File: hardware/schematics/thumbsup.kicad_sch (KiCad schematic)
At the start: 0 parts

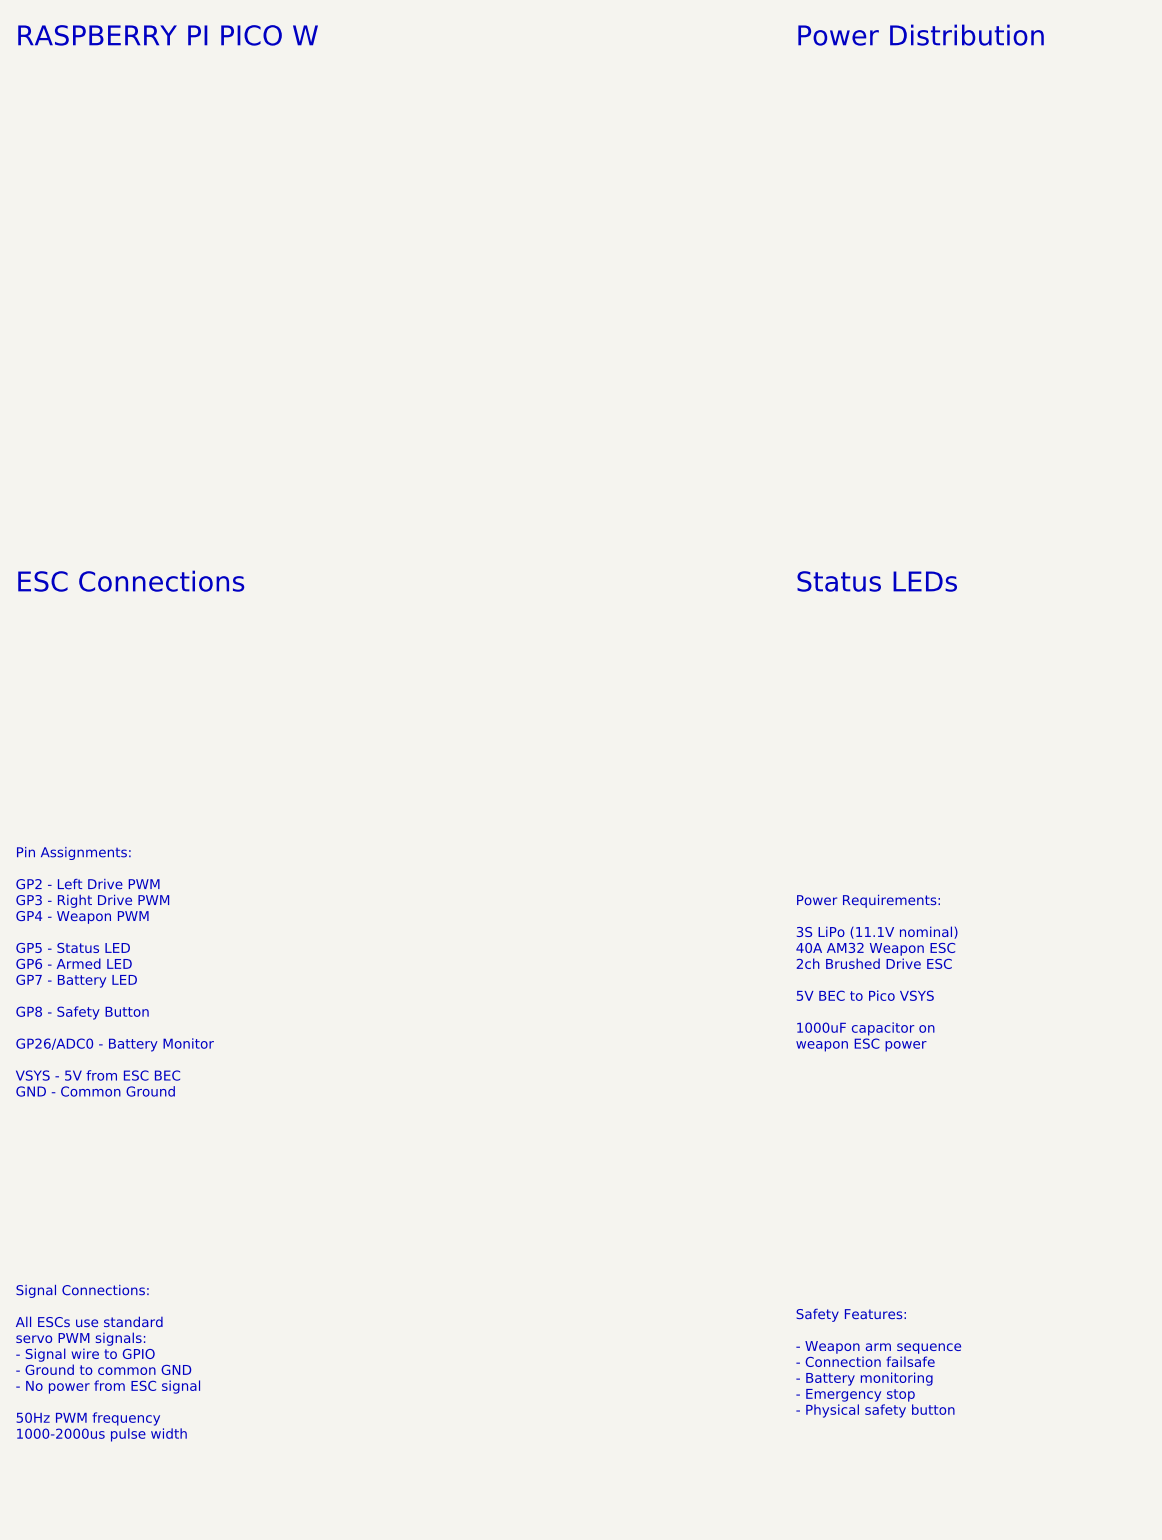
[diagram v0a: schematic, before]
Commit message: fix: Iteration 4 - Race conditions, buffer overflows, synchronization
This commit addresses all 4 CRITICAL and 7 MAJOR code quality issues
identified in the final pre-hardware testing review.

CRITICAL FIXES:

CRITICAL-1: Race condition in weapon_emergency_stop()
- Changed from mode-dependent stop to defense-in-depth approach
- Now executes ALL stop methods (PWM, DShot, GPIO) regardless of mode
- Prevents race where mode could change between read and execution
- Ensures motor stops even if one method fails

CRITICAL-2: Unprotected dshot_initialized flag access
- Made dshot_initialized volatile to prevent compiler reordering
- Flag already protected by mode_mutex in all modification paths
- Prevents use-after-free where weapon_update() could use freed DShot
  resources after mode switch calls dshot_deinit()

CRITICAL-3: Buffer overflow in am32_msp_receive()
- Added buffer_size parameter to function signature
- Validates payload_len from wire against caller's buffer size
- Prevents malicious ESC from overflowing buffer with large payload_len
- Added double-check bounds validation before each write

CRITICAL-4: Infinite loop in am32_passthrough_mode()
- Replaced blocking getchar() with getchar_timeout_us(1000)
- Prevents hang if interrupt consumes char between check and read
- Maintains passthrough functionality with non-blocking reads

MAJOR FIXES:

MAJOR-1: GPIO conflict window in mode switching
- Added comprehensive documentation of race window limitation
- Explained mitigation: single-threaded, mutex-protected, no ISR conflicts
- Added hardware testing requirements for validation

MAJOR-2: Missing NULL checks in dshot_send_throttle()
- Added NULL pointer check for state->pio before dereferencing
- Added validation that state->dma_chan >= 0 before use
- Prevents crashes if state is partially initialized

MAJOR-3: Integer overflow in dshot_throttle_from_percent()
- Rewrote formula to avoid negative intermediates
- Changed from: (percent * range)/100 + offset
- Change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
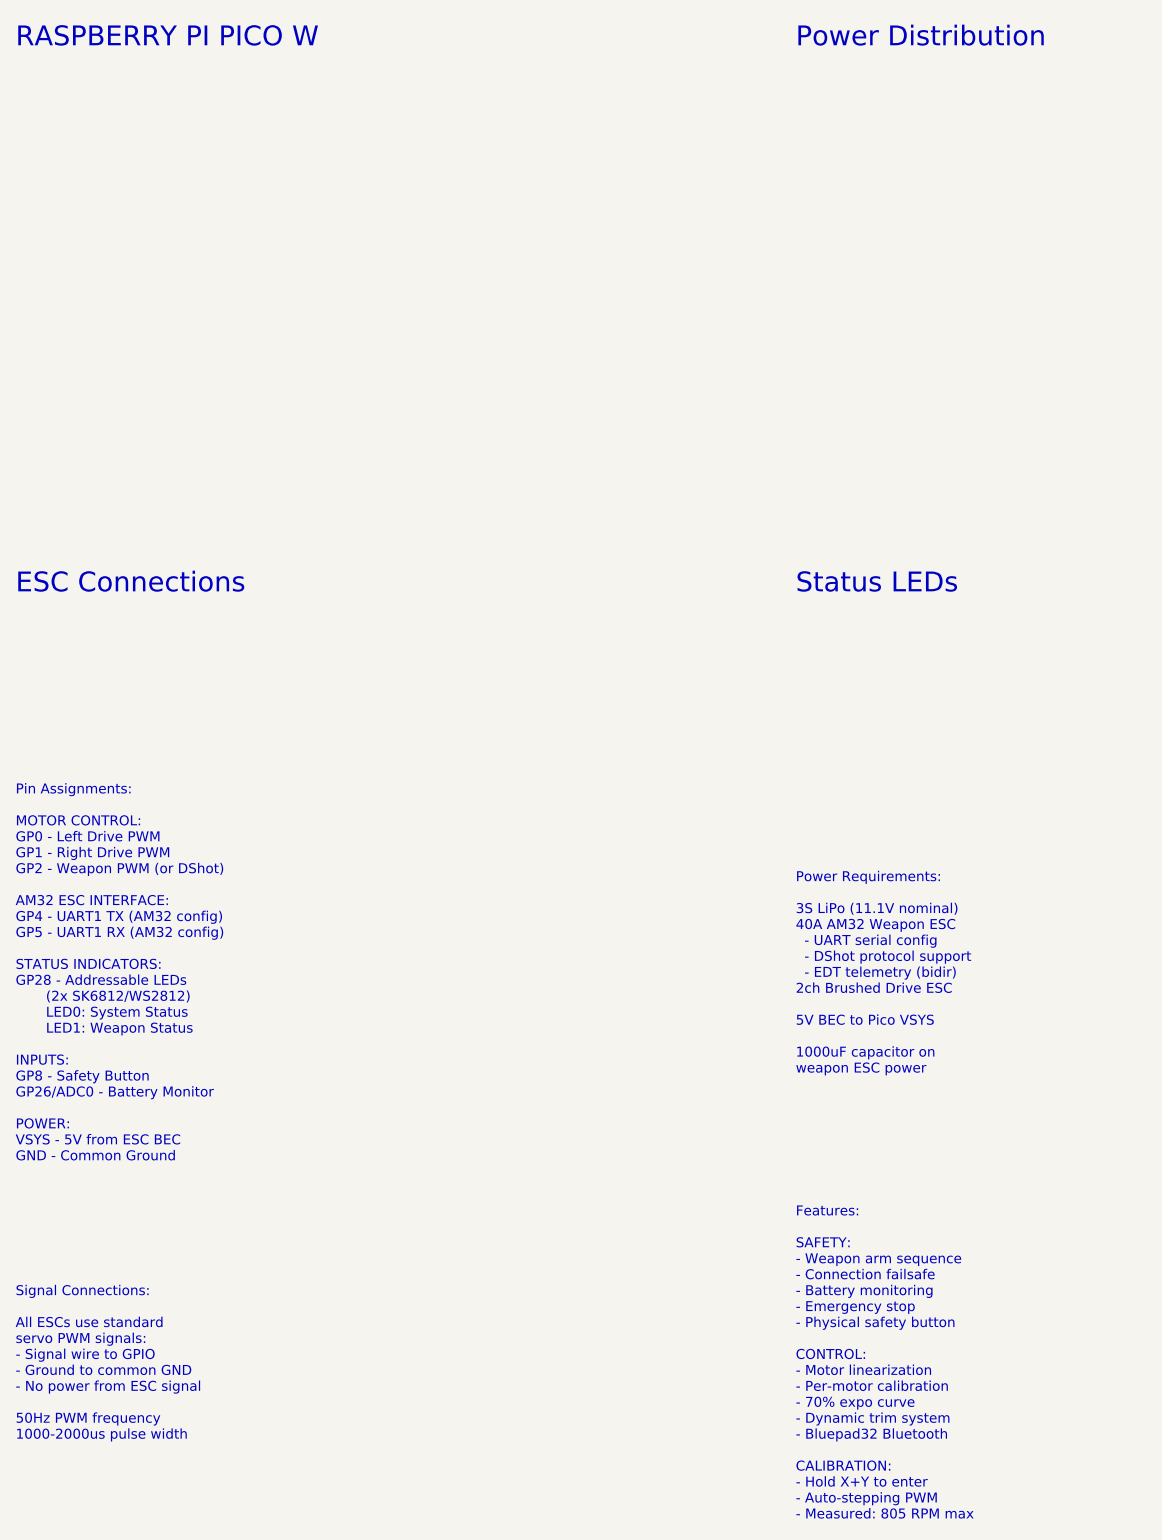
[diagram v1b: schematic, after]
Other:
- note added: "Features: SAFETY: - Weapon arm sequence - Connection failsafe - Battery monitoring - Emergency stop - Physical safety button CONTROL: - Motor linearization - Per-motor calibration - 70% expo curve - Dynamic trim system - Bluepad32 Bluetooth CALIBRATION: - Hold X+Y to enter - Auto-stepping PWM - Measured: 805 RPM max"
- note added: "Pin Assignments: MOTOR CONTROL: GP0 - Left Drive PWM GP1 - Right Drive PWM GP2 - Weapon PWM (or DShot) AM32 ESC INTERFACE: GP4 - UART1 TX (AM32 config) GP5 - UART1 RX (AM32 config) STATUS INDICATORS: GP28 - Addressable LEDs (2x SK6812/WS2812) LED0: System Status LED1: Weapon Status INPUTS: GP8 - Safety Button GP26/ADC0 - Battery Monitor POWER: VSYS - 5V from ESC BEC GND - Common Ground"
- note added: "Power Requirements: 3S LiPo (11.1V nominal) 40A AM32 Weapon ESC - UART serial config - DShot protocol support - EDT telemetry (bidir) 2ch Brushed Drive ESC 5V BEC to Pico VSYS 1000uF capacitor on weapon ESC power"
- note removed: "Pin Assignments: GP2 - Left Drive PWM GP3 - Right Drive PWM GP4 - Weapon PWM GP5 - Status LED GP6 - Armed LED GP7 - Battery LED GP8 - Safety Button GP26/ADC0 - Battery Monitor VSYS - 5V from ESC BEC GND - Common Ground"
- note removed: "Power Requirements: 3S LiPo (11.1V nominal) 40A AM32 Weapon ESC 2ch Brushed Drive ESC 5V BEC to Pico VSYS 1000uF capacitor on weapon ESC power"
- note removed: "Safety Features: - Weapon arm sequence - Connection failsafe - Battery monitoring - Emergency stop - Physical safety button"
- title: Antweight Combat Robot Control System -> ThumbsUp - Antweight Combat Robot Control System
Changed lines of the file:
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@@
-(kicad_sch (version 20211123) (generator eeschema)
-  (paper "A4")
-  (title_block
-    (title "Antweight Combat Robot Control System")
-    (date "2025-01-16")
-    (rev "1.0")
-    (company "ThumbsUp Robot")
-    (comment 1 "Raspberry Pi Pico W based combat robot controller")
-    (comment 2 "3S LiPo powered with brushed drive and brushless weapon")
-  )
-  (text "RASPBERRY PI PICO W" (at 50 30 0)
-    (effects (font (size 2.54 2.54)) (justify left))
-  )
-  (text "Power Distribution" (at 150 30 0)
-    (effects (font (size 2.54 2.54)) (justify left))
-  )
-  (text "ESC Connections" (at 50 100 0)
-    (effects (font (size 2.54 2.54)) (justify left))
-  )
-  (text "Status LEDs" (at 150 100 0)
-    (effects (font (size 2.54 2.54)) (justify left))
-  )
-  (text "Pin Assignments:\n\nGP2 - Left Drive PWM\nGP3 - Right Drive PWM\nGP4 - Weapon PWM\n\nGP5 - Status LED\nGP6 - Armed LED\nGP7 - Battery LED\n\nGP8 - Safety Button\n\nGP26/ADC0 - Battery Monitor\n\nVSYS - 5V from ESC BEC\nGND - Common Ground" (at 50 150 0)
-    (effects (font (size 1.27 1.27)) (justify left))
-  )
-  (text "Power Requirements:\n\n3S LiPo (11.1V nominal)\n40A AM32 Weapon ESC\n2ch Brushed Drive ESC\n\n5V BEC to Pico VSYS\n\n1000uF capacitor on\nweapon ESC power" (at 150 150 0)
-    (effects (font (size 1.27 1.27)) (justify left))
-  )
-  (text "Signal Connections:\n\nAll ESCs use standard\nservo PWM signals:\n- Signal wire to GPIO\n- Ground to common GND\n- No power from ESC signal\n\n50Hz PWM frequency\n1000-2000us pulse width" (at 50 200 0)
-    (effects (font (size 1.27 1.27)) (justify left))
-  )
-  (text "Safety Features:\n\n- Weapon arm sequence\n- Connection failsafe\n- Battery monitoring\n- Emergency stop\n- Physical safety button" (at 150 200 0)
-    (effects (font (size 1.27 1.27)) (justify left))
-  )
+(kicad_sch
+	(version 20250114)
+	(generator "eeschema")
+	(generator_version "9.0")
+	(paper "A4")
+	(title_block
+		(title "ThumbsUp - Antweight Combat Robot Control System")
+		(date "2025-11-18")
+		(rev "1.2")
+		(company "ThumbsUp Robot")
+		(comment 1 "Raspberry Pi Pico W with Bluepad32 Bluetooth controller")
+		(comment 2 "3S LiPo powered with brushed drive motors and brushless weapon")
+		(comment 3 "AM32 ESC integration with DShot and serial configuration")
+	)
+	(text "Power Requirements:\n\n3S LiPo (11.1V nominal)\n40A AM32 Weapon ESC\n  - UART serial config\n  - DShot protocol support\n  - EDT telemetry (bidir)\n2ch Brushed Drive ESC\n\n5V BEC to Pico VSYS\n\n1000uF capacitor on\nweapon ESC power"
+		(exclude_from_sim no)
+		(at 150 150 0)
+		(effects
+			(font
+				(size 1.27 1.27)
+			)
+			(justify left)
+		)
+	)
+	(text "Pin Assignments:\n\nMOTOR CONTROL:\nGP0 - Left Drive PWM\nGP1 - Right Drive PWM\nGP2 - Weapon PWM (or DShot)\n\nAM32 ESC INTERFACE:\nGP4 - UART1 TX (AM32 config)\nGP5 - UART1 RX (AM32 config)\n\nSTATUS INDICATORS:\nGP28 - Addressable LEDs\n       (2x SK6812/WS2812)\n       LED0: System Status\n       LED1: Weapon Status\n\nINPUTS:\nGP8 - Safety Button\nGP26/ADC0 - Battery Monitor\n\nPOWER:\nVSYS - 5V from ESC BEC\nGND - Common Ground"
+		(exclude_from_sim no)
+		(at 50 150 0)
+		(effects
+			(font
+				(size 1.27 1.27)
+			)
+			(justify left)
+		)
+	)
+	(text "Signal Connections:\n\nAll ESCs use standard\nservo PWM signals:\n- Signal wire to GPIO\n- Ground to common GND\n- No power from ESC signal\n\n50Hz PWM frequency\n1000-2000us pulse width"
+		(exclude_from_sim no)
+		(at 50 200 0)
+		(effects
+			(font
+				(size 1.27 1.27)
+			)
+			(justify left)
+		)
+	)
+	(text "Power Distribution"
+		(exclude_from_sim no)
+		(at 150 30 0)
+		(effects
+			(font
+				(size 2.54 2.54)
+			)
+			(justify left)
+		)
+	)
+	(text "ESC Connections"
+		(exclude_from_sim no)
+		(at 50 100 0)
+		(effects
+			(font
+				(size 2.54 2.54)
+			)
+			(justify left)
+		)
+	)
+	(text "Status LEDs"
+		(exclude_from_sim no)
+		(at 150 100 0)
+		(effects
+			(font
+				(size 2.54 2.54)
+			)
+			(justify left)
+		)
+	)
+	(text "RASPBERRY PI PICO W"
+		(exclude_from_sim no)
+		(at 50 30 0)
+		(effects
+			(font
+				(size 2.54 2.54)
+			)
+			(justify left)
+		)
+	)
+	(text "Features:\n\nSAFETY:\n- Weapon arm sequence\n- Connection failsafe\n- Battery monitoring\n- Emergency stop\n- Physical safety button\n\nCONTROL:\n- Motor linearization\n- Per-motor calibration\n- 70% expo curve\n- Dynamic trim system\n- Bluepad32 Bluetooth\n\nCALIBRATION:\n- Hold X+Y to enter\n- Auto-stepping PWM\n- Measured: 805 RPM max"
+		(exclude_from_sim no)
+		(at 150 200 0)
+		(effects
+			(font
+				(size 1.27 1.27)
+			)
+			(justify left)
+		)
+	)
+	(sheet_instances
+		(path "/"
+			(page "1")
+		)
+	)
+	(embedded_fonts no)
 )
